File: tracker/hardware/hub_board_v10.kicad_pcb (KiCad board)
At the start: 2 copper layers, 72 x 80 mm, 28 parts, among them U1 U1, U2 U2, U3 U3, U5 U5, U6 U6, U7 U7

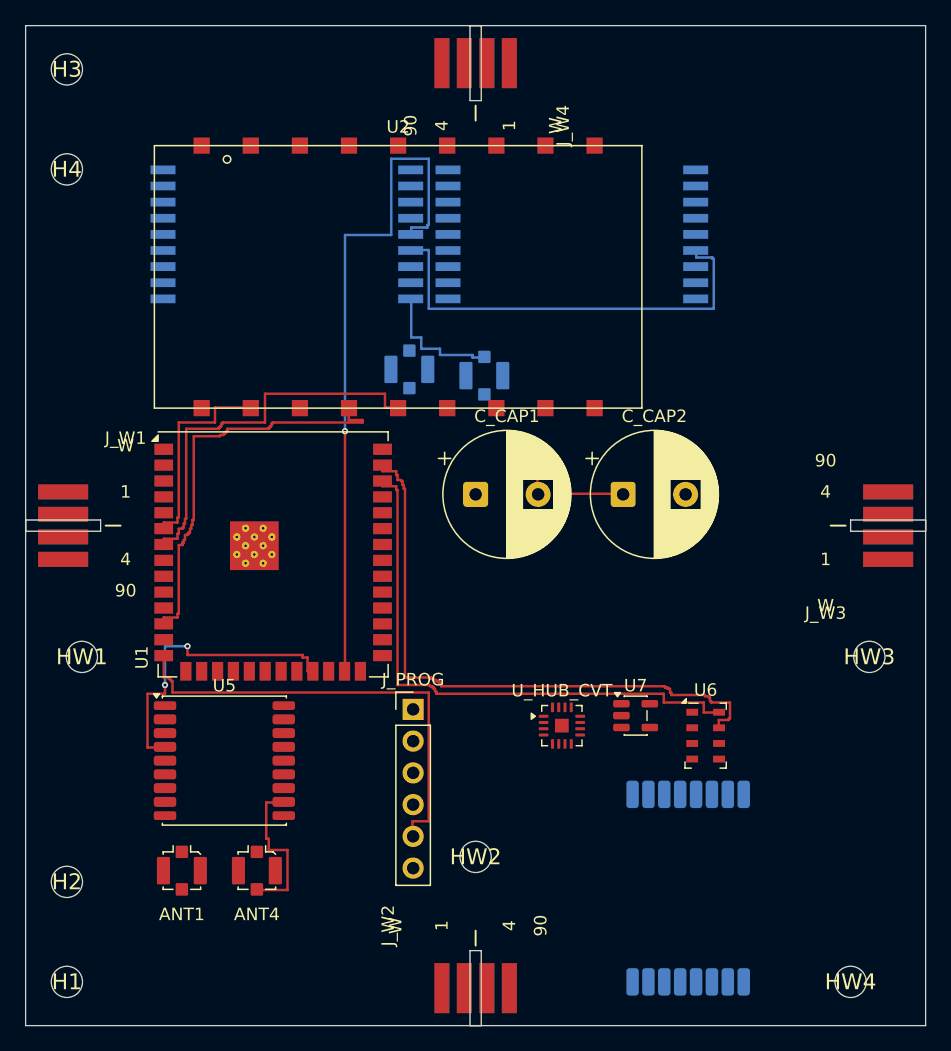
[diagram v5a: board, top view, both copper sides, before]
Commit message: feat(v10): --max-expansions restored (lost in a revert) + finer grid MEASURED as a real lever
RESTORED: --max-expansions. It had been dropped by one of my earlier `git checkout` reverts, so
a scheduled sweep silently died with "unrecognized arguments: --max-expansions" and I nearly
read the empty log as a result. Checked the help output before trusting the run.

B35 -- grid pitch is a ROUTING-QUALITY LEVER, not just a speed knob. Measured on the SPI2 trio
(the three data lines that must all escape U1's congested west side):

  pitch 0.10mm, cap 2M   -> 1 of 3 routed  (SPI2_MISO only)
  pitch 0.10mm, cap 5M   -> 1 of 3 routed  (cap is NOT the constraint)
  pitch 0.05mm, cap 5M   -> 2 of 3 routed  (SPI2_MISO + SPI2_MOSI)

The 0.05mm grid resolves a fan-out the 0.10mm grid cannot. Cost: ~4x the cells, so a full
route takes minutes rather than ~90s. This is a SEARCH resolution change -- output tracks are
still 0.2mm wide and the board is unchanged -- so it needs no ADR, no placement change and no
extra copper layers.

STATE: a full route at pitch 0.05 was still running when this was committed (>10min). Its
result is NOT claimed here. What IS measured: the trio goes 1/3 -> 2/3 at the finer pitch.

CORRECTION CARRIED FORWARD: the earlier "layout limit proven three ways" conclusion stays
WITHDRAWN (bug B34). The remaining evidence for a genuine limit is weaker than it looked: the
trio improves with search resolution, which a hard geometric limit would not do.
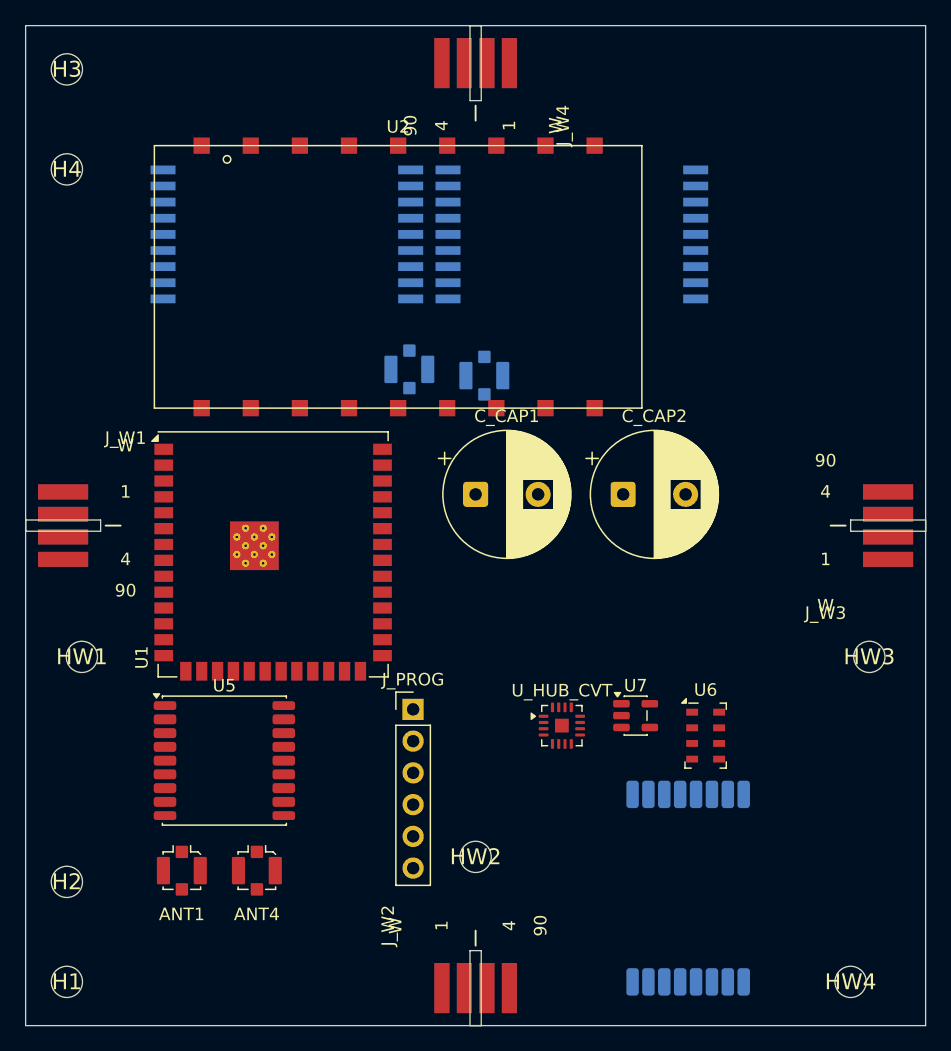
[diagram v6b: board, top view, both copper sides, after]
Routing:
- net /U3_RESET_N: track 55.2 -> 0.00 mm, vias 1 -> 0
- net /I2C_SDA: track 49.7 -> 0.00 mm
- net /I2C_SCL: track 45.4 -> 0.00 mm
- net /USB_DP: track 37.0 -> 0.00 mm
- net /VTCXO_VNTC: track 35.0 -> 0.00 mm
- net /F33_BUSY: track 34.3 -> 0.00 mm
- net /F33_CS_N: track 31.9 -> 0.00 mm
- net /GNSS_PPS: track 24.7 -> 0.00 mm, vias 2 -> 0
- net /SPI2_MISO: track 16.7 -> 0.00 mm
- net /ANT4_GNSS_L1: track 12.6 -> 0.00 mm
- net /ANT3_2G4_RX: track 10.6 -> 0.00 mm
- net /SCAP_MID: track 9.80 -> 0.00 mm

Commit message: feat(v10): escalating-resolution route (B36-B39) -- 14 nets, but E28_BUSY still flags 2 crossings (NOT claimed clean)
B36 -- route_escalating.sh: coarse pass at pitch 0.10, then retry ONLY the failures at pitch
  0.05 via --append. Motivated by measurement: a full 0.05 route does not finish (700s
  timeout, no output) because every net pays the 4x cell cost even when it routes trivially at
  0.1. The finer grid genuinely recovers nets (SPI2 trio 1/3 -> 2/3), so use it only where
  needed. MEASURED: pass1 12-13 nets, pass2 +2 to +3.
B37 -- --append loaded existing copper for VALIDATION but never marked it into the A* GRID, so
  the search routed straight through it and every candidate was rejected ("self-check:
  isolation vs routed ..."). Measured: pass 2 retried 12 nets and routed 0. Fixed by marking
  existing tracks into the grid at CLEAR + TRACK_W. Same failure class as B34, different site.
  Also had to MOVE the marking block after build_grid() -- it referenced nx/ny before they
  existed (UnboundLocalError, caught on the first run).
B38 -- the under-body check in validate_plan was PER SEGMENT (`L * inside / steps > 0.5`). At
  fine pitch each zigzag segment is ~0.05mm, so every segment passed while the route tunnelled
  through the keep-out: measured /E28_BUSY running 5.71mm beneath U_E28 and accepted by the
  router, caught only by the gate afterwards. Now the inside-length is ACCUMULATED over the
  whole plan.
B39 -- the own-pad exemption in the under-body check was a 2.0mm halo around every own pad. For
  a pad on the keep-out module's BOUNDARY (E28 pads sit on the module edge, opening outward)
  that halo reaches INSIDE the module, exempting a route along the pad row. Shrunk to 0.6mm.

MEASURED STATE (NOT CLEAN -- stated plainly):
  pass1 12 nets + pass2 2 nets = 14 nets, 214 tracks, 6 vias
  check_lane_clearance 0 · integrity 0 · isolation 0 · lane-vs-pad 0 · cross-side 0 · holes 0
  geometry 0
  check_copper_under_body: crossings 2 -- /E28_BUSY still run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
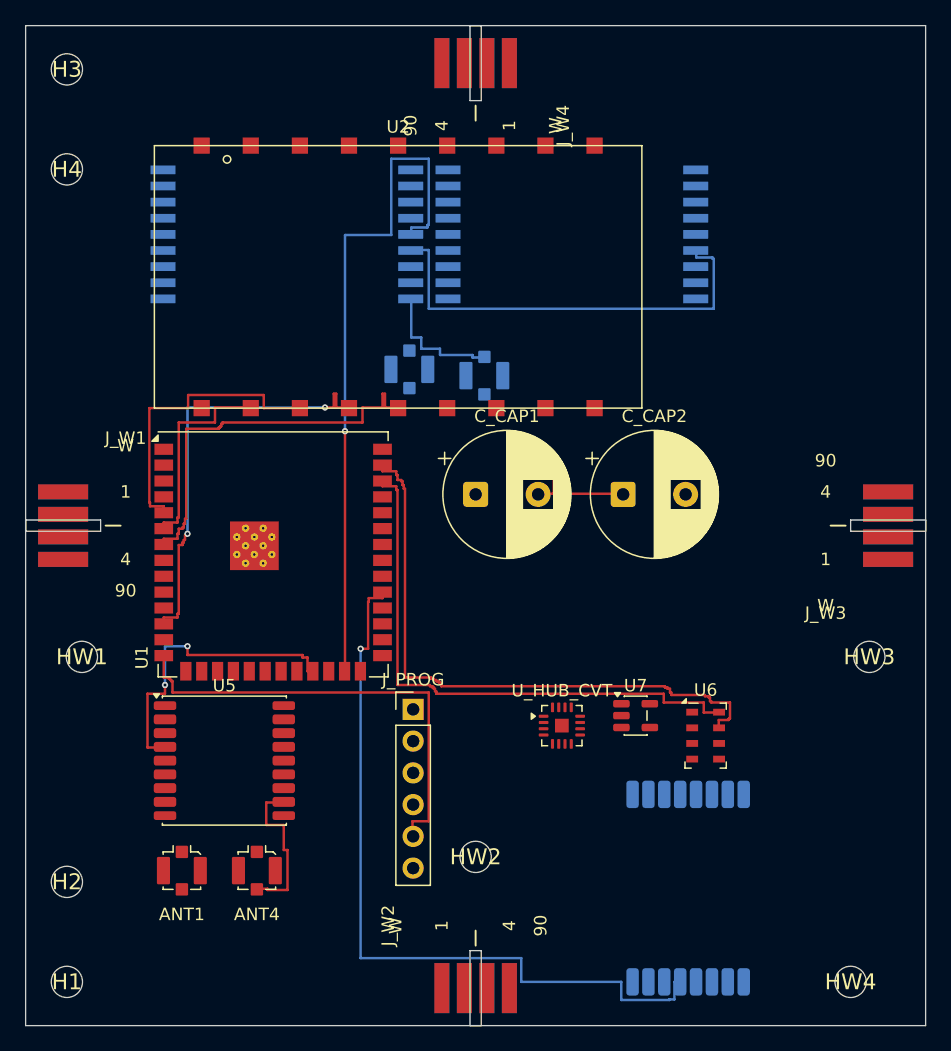
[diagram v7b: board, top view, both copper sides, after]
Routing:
- net /E28_BUSY: track 0.00 -> 61.4 mm, vias 0 -> 1
- net /U3_RESET_N: track 0.00 -> 55.2 mm, vias 0 -> 1
- net /I2C_SDA: track 0.00 -> 49.7 mm
- net /I2C_SCL: track 0.00 -> 45.4 mm
- net /USB_DP: track 0.00 -> 37.0 mm
- net /VTCXO_VNTC: track 0.00 -> 35.0 mm
- net /F33_BUSY: track 0.00 -> 34.3 mm, vias 0 -> 2
- net /F33_CS_N: track 0.00 -> 31.9 mm
- net /GNSS_PPS: track 0.00 -> 24.7 mm, vias 0 -> 2
- net /SPI2_MOSI: track 0.00 -> 23.7 mm
- net /SPI2_MISO: track 0.00 -> 16.7 mm
- net /ANT4_GNSS_L1: track 0.00 -> 12.6 mm
- net /ANT3_2G4_RX: track 0.00 -> 10.6 mm
- net /SCAP_MID: track 0.00 -> 9.80 mm

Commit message: fix(v10): B40 -- keep-out body was the PAD FIELD, not the module courtyard; /E28_BUSY fixed
THE BUG. The router's own under-body check used a body rect built from the footprint's PAD
FIELD. For the E28 that is (48.06, 60.40)-(57.95, 77.60), while the module's courtyard is
(41.93, 60.38)-(64.08, 77.63). The pad-field rect left an UNCOVERED STRIP x 41.93..48.06, and
/E28_BUSY's 8.00mm run at y=76.5 sat exactly in it. So:
  * validate_plan NEVER SAW the crossing (its body rect was too small) -> the router emitted a
    keep-out violation and considered the net successfully routed;
  * the GATE caught it (the gate uses the courtyard) -> "UNDER BODY 5.71mm: /E28_BUSY track
    runs beneath U_E28", reported in the previous commit as an OPEN defect.
A keep-out means the whole MODULE, not the pad field. Keep-out refs now use the courtyard.

MEASURED AFTER: /E28_BUSY routed, and the router REFUSES the crossing itself --
check_copper_under_body crossings 2 -> 0.

FULLY CLEAN STATE, all EIGHT gates zero:
  pass 1 (pitch 0.10) 12 nets + pass 2 (pitch 0.05, --append) 3 nets = 15 nets
  268 tracks, 7 vias
  check_board_geometry        0  28 footprints in bounds, 0 same-side overlaps
  check_hole_clearance        0
  check_lane_clearance        0  UNDER-CLEARANCE 0
  check_lane_integrity        0  VIOLATIONS 0
  check_copper_under_body     0  crossings 0        <-- was 2
  check_lane_isolation        0  ISOLATION VIOLATIONS 0
  check_cross_side_collision  0  PAD SHORTS ACROSS SIDES 0
  check_lane_vs_pad_layer     0  HARD DEFECTS 0

SESSION BUG LEDGER (B32-B40, all introduced by me, all found by measurement):
  B32 via-table flat index row[i] vs row[j*nx+i]      -> router placed ZERO vias
  B34 isolation obstacle under-marked 0.10mm          -> A* found paths, validator discarded
  B37 --append didn't mark existing copper as A* obstacles -> pass 2 routed 0 of 12
  B38 under-body check PER SEGMENT                    -> tunnelled 5.71mm through the keep-out
  B39 own-pad exemption 2.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
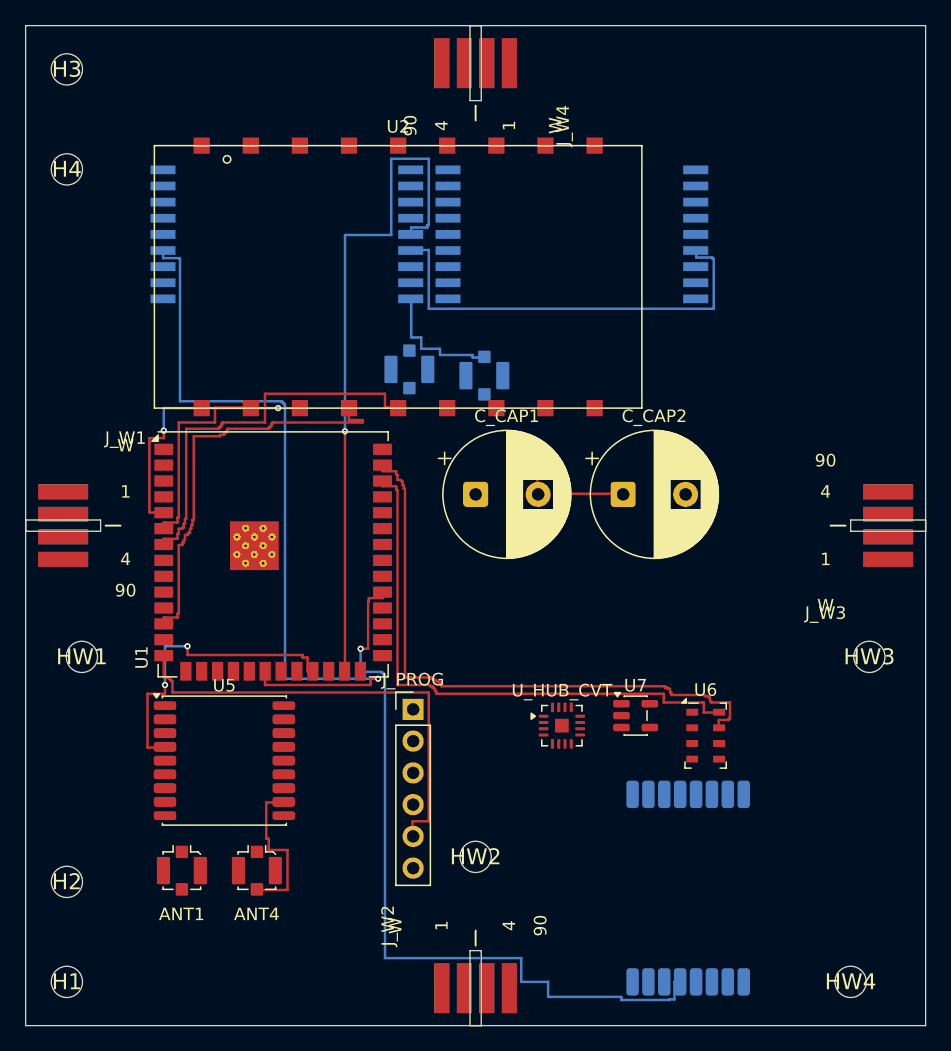
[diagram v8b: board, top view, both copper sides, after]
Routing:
- net /U3_CS_N: track 0.00 -> 62.1 mm, vias 0 -> 1
- net /SPI2_MOSI: track 23.7 -> 21.6 mm, vias 0 -> 2
- net /F33_BUSY: vias 2 -> 0
